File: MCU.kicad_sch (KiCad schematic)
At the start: 31 parts, among them J3 Conn_ARM_SWD_TagConnect_TC2030, U1 MLPF-WB55-01E3, U5 STM32WB55CGUx, U7 FM24CL16B, X1 32MHz, X2 32kHz768

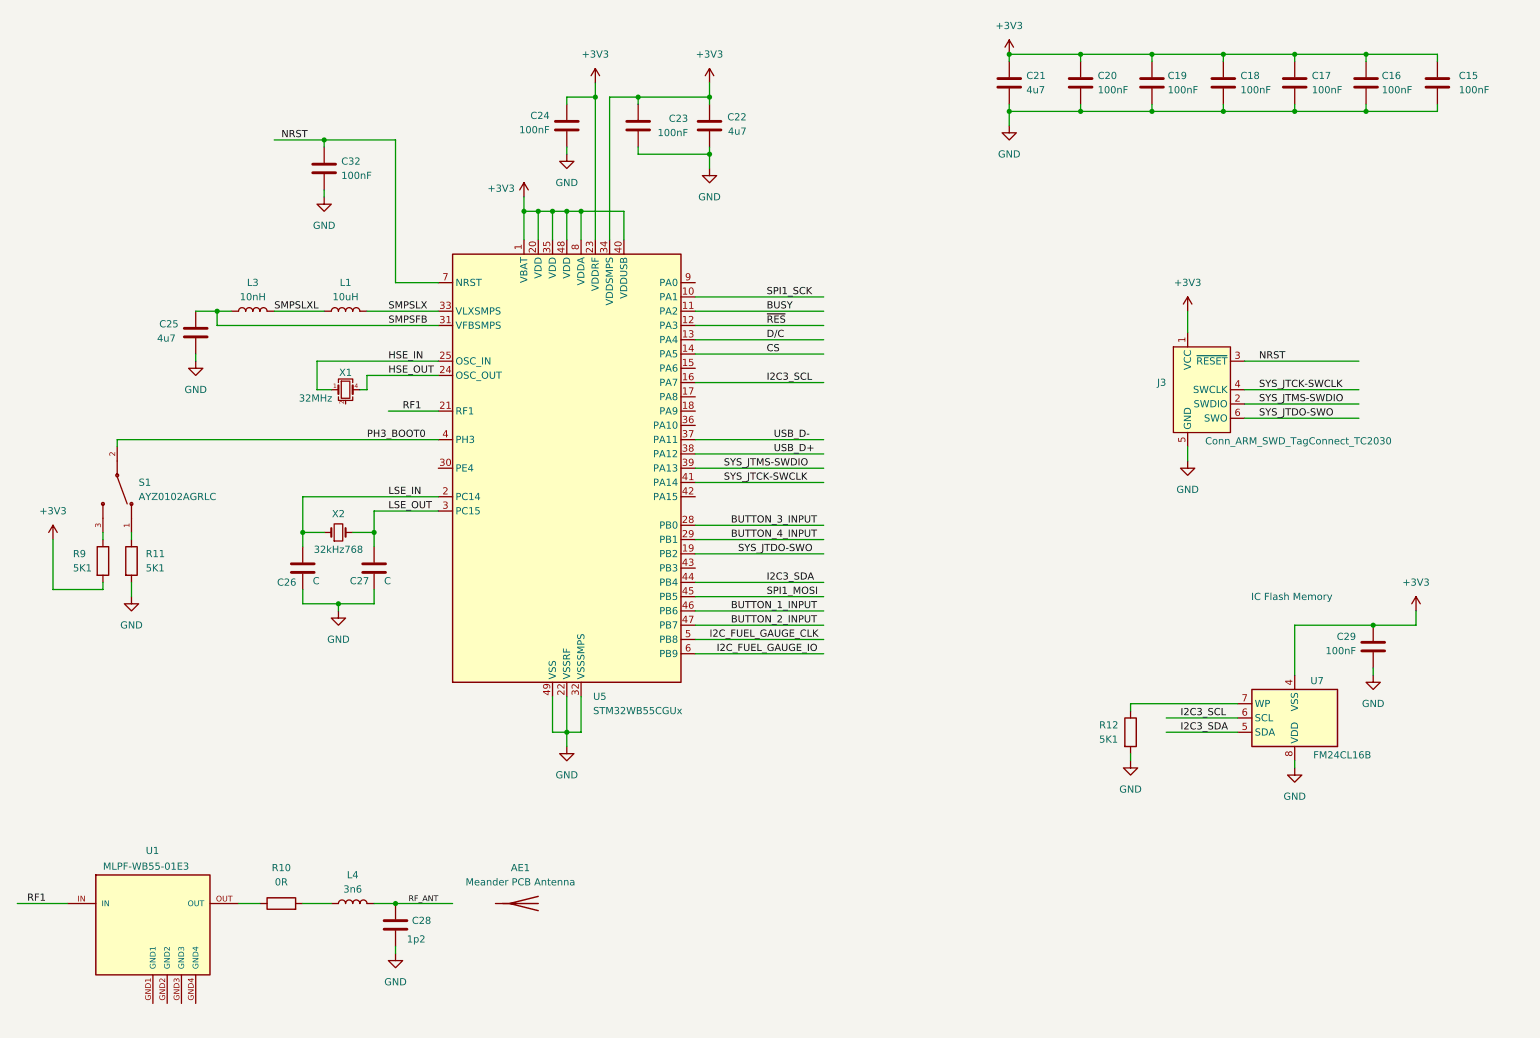
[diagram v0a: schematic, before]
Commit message: cleaned up some net labels for ERC
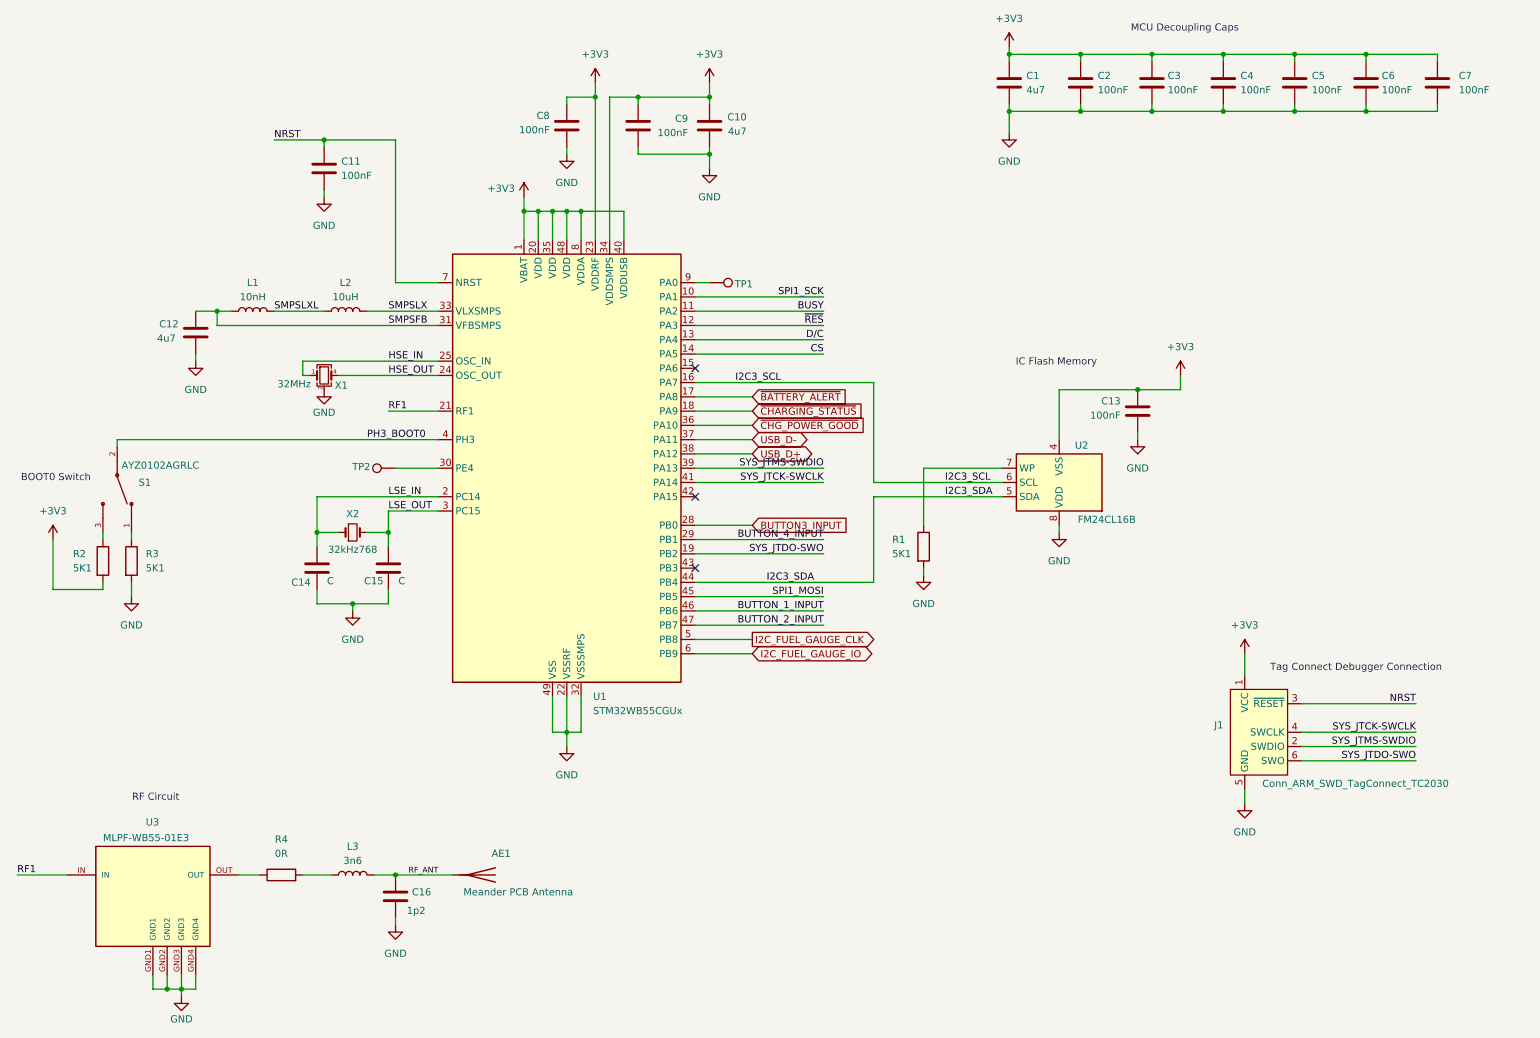
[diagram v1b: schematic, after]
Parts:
- added TP1, TP2: ~, symbol Connector:TestPoint
- renumbered C21 to C1, C22 to C10, C32 to C11, C25 to C12, C29 to C13, C26 to C14, C27 to C15, C28 to C16, C20 to C2, C19 to C3, C18 to C4, C17 to C5, C16 to C6, C15 to C7, C24 to C8, C23 to C9, J3 to J1, L3 to L1, L1 to L2, L4 to L3, R12 to R1, R9 to R2, R11 to R3, R10 to R4, U5 to U1, U7 to U2, U1 to U3
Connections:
- net GND: now also U3.GND1, U3.GND2, U3.GND3, U3.GND4, X1.2 (G), X1.3 (G)
- net RF_ANT: now also AE1.1 (A)
- net ~{BATTERY_ALERT}: now reaches U1.17 (PA8)
- net ~{CHARGING_STATUS}: now reaches U1.18 (PA9)
- net at U1.30 (PE4): now also TP2.1
- net ~{CHG_POWER_GOOD}: now reaches U1.36 (PA10)
- net at U1.9 (PA0): now also TP1.1
- net BUTTON_3_INPUT renamed BUTTON3_INPUT
- no-connect marks 0 -> 3
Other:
- note added: "BOOT0 Switch"
- note added: "MCU Decoupling Caps"
- note added: "RF Circuit"
- note added: "Tag Connect Debugger Connection"
- moved on the sheet: AE1, C13, C14, C15, C16, J1, L3, R1, R4, U2, U3, X1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

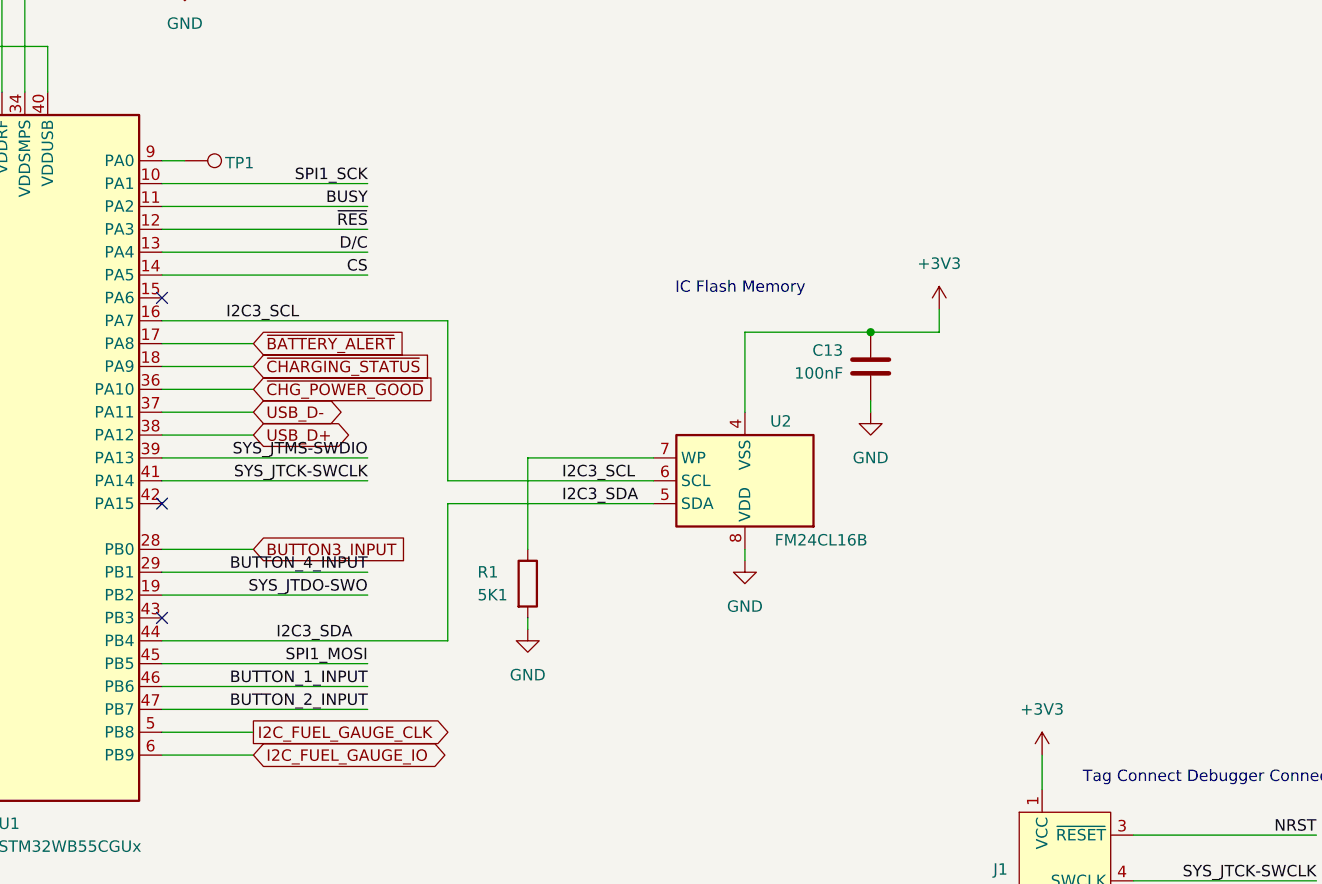
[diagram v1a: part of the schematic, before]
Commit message: Cleaned up local vs. global net labels
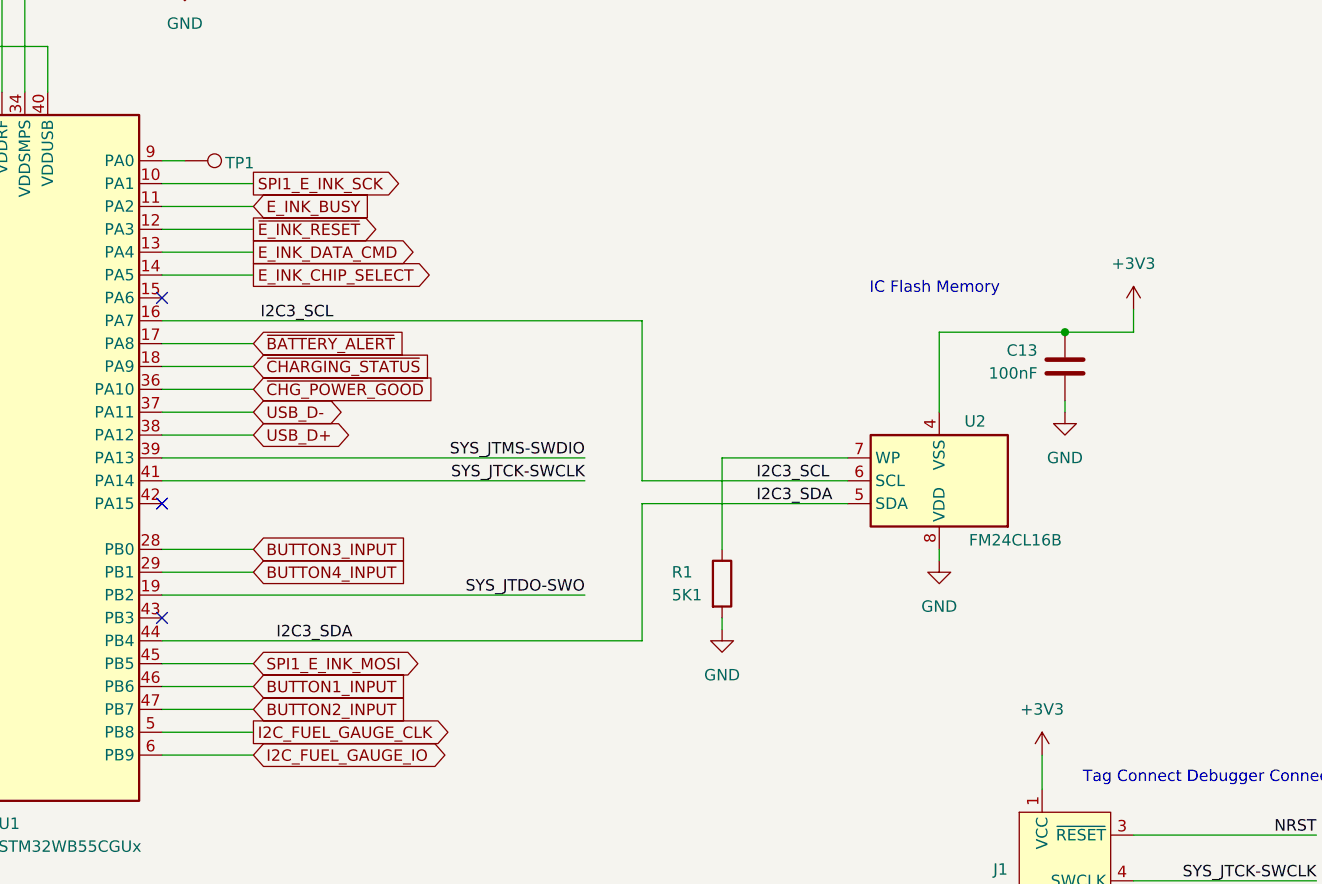
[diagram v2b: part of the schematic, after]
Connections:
- net BUSY renamed E_INK_BUSY
- net BUTTON_1_INPUT renamed BUTTON1_INPUT
- net BUTTON_2_INPUT renamed BUTTON2_INPUT
- net BUTTON_4_INPUT renamed BUTTON4_INPUT
- net CS renamed E_INK_CHIP_SELECT
- net D/C renamed E_INK_DATA_CMD
- net SPI1_MOSI renamed SPI1_E_INK_MOSI
- net SPI1_SCK renamed SPI1_E_INK_SCK
- net ~{RES} renamed ~{E_INK_RESET}
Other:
- moved on the sheet: C13, R1, U2

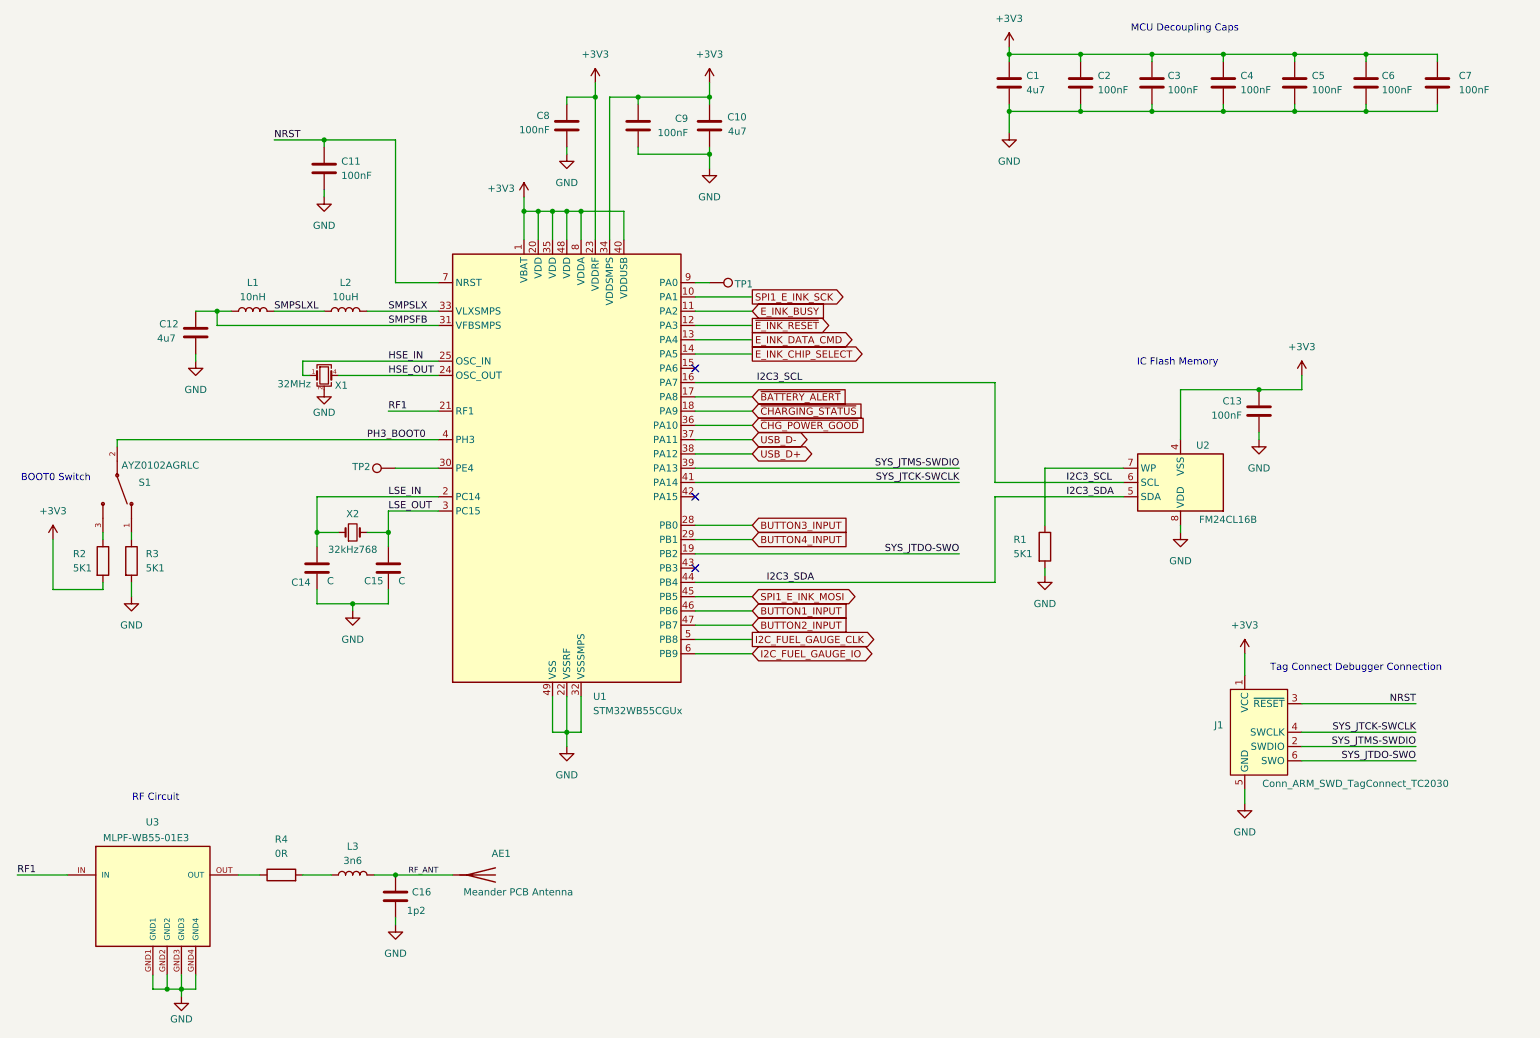
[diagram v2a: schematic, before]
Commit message: ERC Check fixes
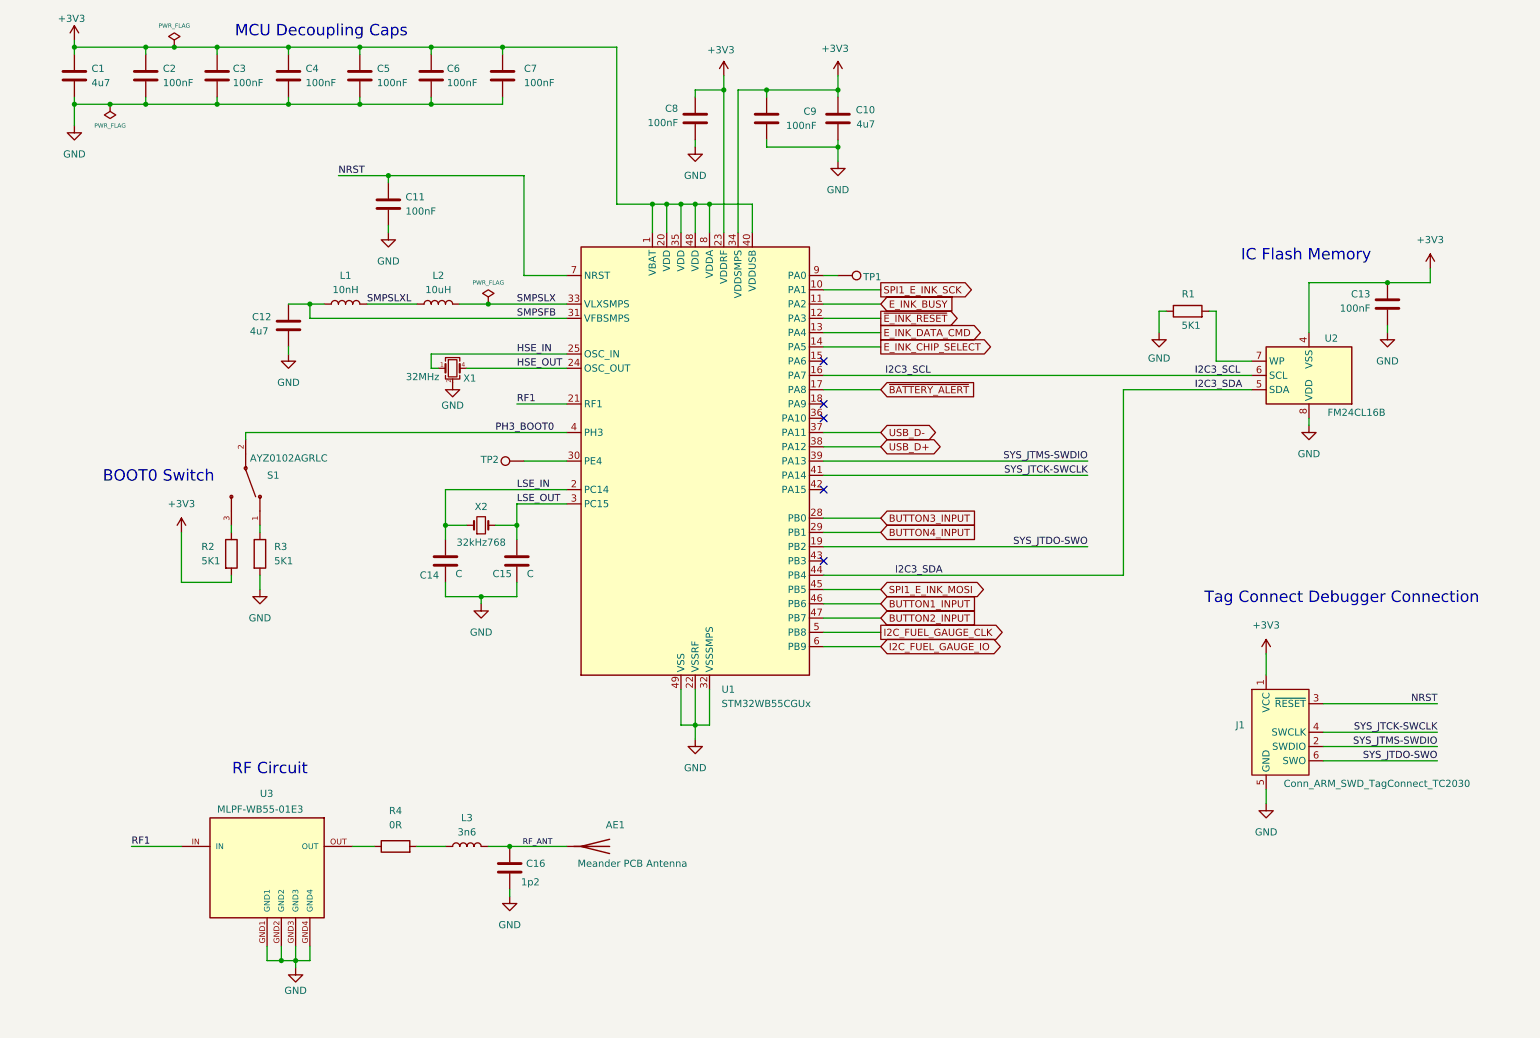
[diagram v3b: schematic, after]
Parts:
- S1: footprint AYZ0102AGRLC:SW_AYZ0102AGRLC -> LibraryFootprints:SW_AYZ0102AGRLC
- U3: footprint MLPF-WB55-01E3:MLPF-WB55-01E3 -> LibraryFootprints:MLPF-WB55-01E3
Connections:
- net GND: now also R1.1; no longer R1.2
- net at U2.7 (WP): now also R1.2; no longer R1.1
- net ~{CHARGING_STATUS}: no longer names the net of U1.18 (PA9)
- net ~{CHG_POWER_GOOD}: no longer names the net of U1.36 (PA10)
- no-connect marks 3 -> 5
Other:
- moved on the sheet: AE1, C1, C10, C11, C12, C13, C14, C15, C16, C2, C3, C4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
